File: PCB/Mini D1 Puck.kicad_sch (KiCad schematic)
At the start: 20 parts, among them J1 Regulator, J2 Charger, M1 VI1, M2 VI2, M3 VI3, M4 VI4, Q1 2N2222, Q2 2N2222, SW1 SW_SPDT, SW2 RST SW, U1 WEMOS_D1_mini

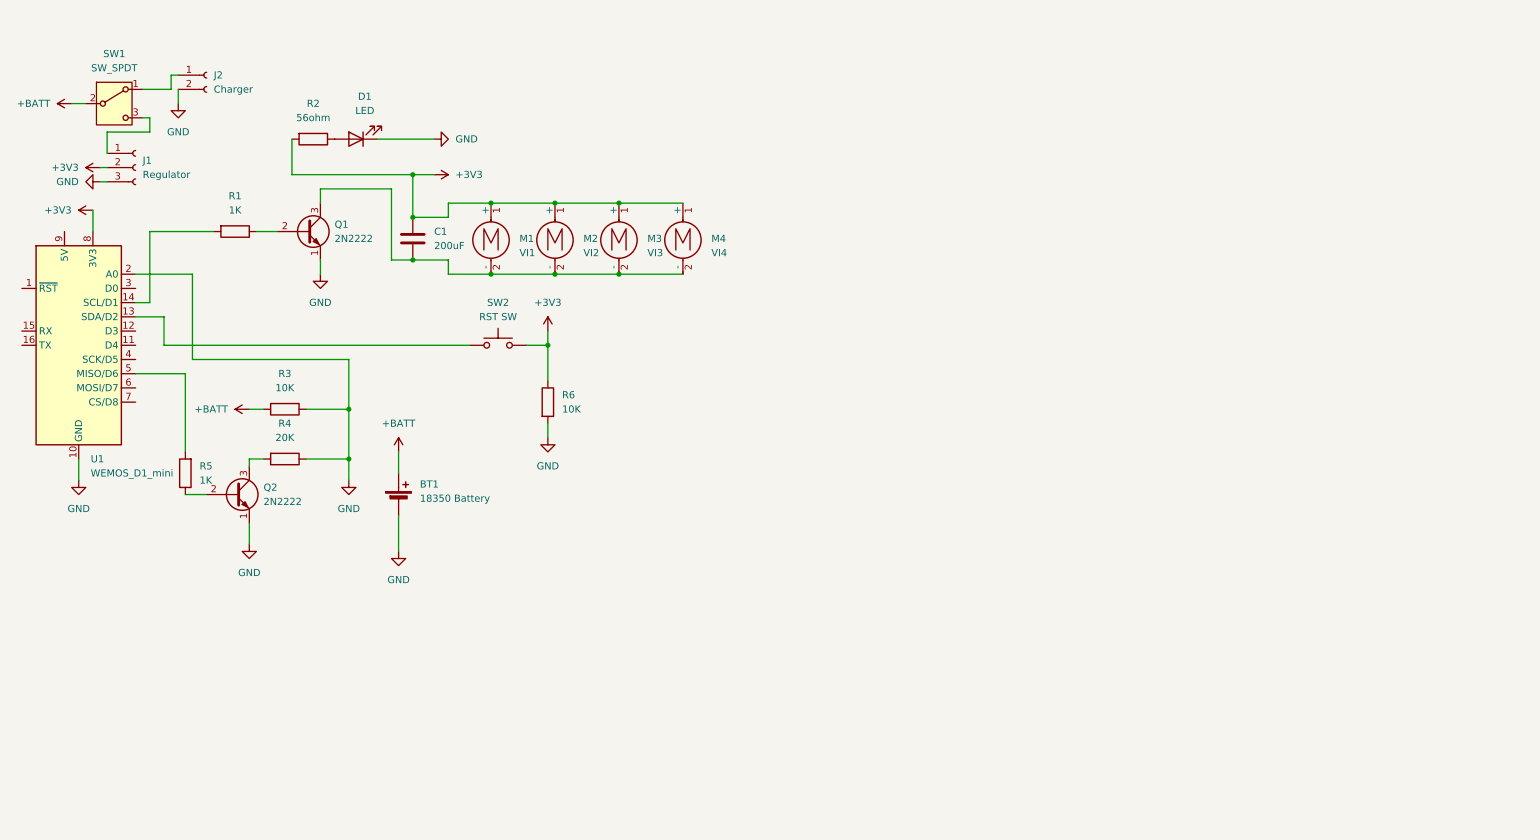
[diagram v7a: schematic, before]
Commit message: Work on new schematic, up minimum voltage in firmware
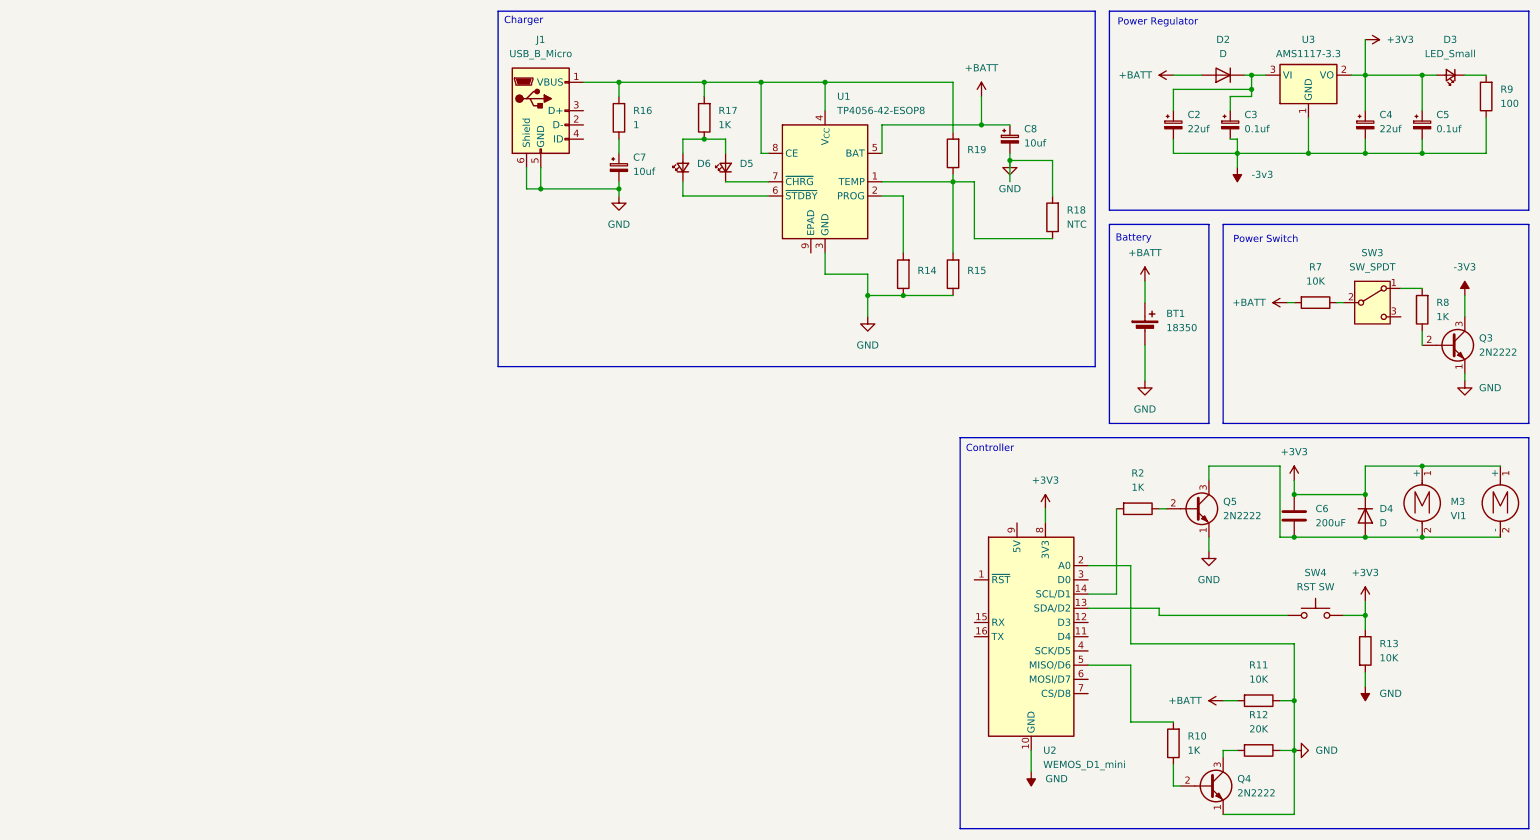
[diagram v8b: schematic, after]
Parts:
- removed C1: 200uF, symbol Device:C
- removed D1: LED, symbol Device:LED
- removed J1: Regulator, symbol Connector:Conn_01x03_Socket
- removed J2: Charger, symbol Connector:Conn_01x02_Socket
- removed M1: VI1, symbol Motor:Motor_DC
- removed M2: VI2, symbol Motor:Motor_DC
- removed Q1, Q2: 2N2222, symbol Transistor_BJT:Q_NPN_EBC
- removed R1, R5: 1K, symbol Device:R
- removed R3, R6: 10K, symbol Device:R
- removed R4: 20K, symbol Device:R
- removed SW1: SW_SPDT, symbol Switch:SW_SPDT
- removed SW2: RST SW, symbol Switch:SW_Push
- removed U1: WEMOS_D1_mini, RF_Module:WEMOS_D1_mini_light, symbol RF_Module:WEMOS_D1_mini
- added C2, C4: 22uf, symbol Device:C_Polarized_Small
- added C3, C5: 0.1uf, symbol Device:C_Polarized_Small
- added C6: 200uF, symbol Device:C
- added C7, C8: 10uf, symbol Device:C_Polarized_Small
- added D2, D4: D, symbol Device:D
- added D3: LED_Small, symbol Device:LED_Small
- added D5, D6: ~, symbol Device:LED_Small
- added J1: USB_B_Micro, symbol Connector:USB_B_Micro
- added Q3, Q4, Q5: 2N2222, symbol Transistor_BJT:Q_NPN_EBC
- added R10, R17, R8: 1K, symbol Device:R
- added R11, R13, R7: 10K, symbol Device:R
- added R12: 20K, symbol Device:R
- added R14, R15, R19: ~, symbol Device:R
- added R16: 1, symbol Device:R
- added R18: NTC, symbol Device:R
- added R9: 100, symbol Device:R
- added SW3: SW_SPDT, symbol Switch:SW_SPDT
- added SW4: RST SW, symbol Switch:SW_Push
- added U1: TP4056-42-ESOP8, Package_SO:SOIC-8-1EP_3.9x4.9mm_P1.27mm_EP2.41x3.3mm_ThermalVias, symbol Battery_Management:TP4056-42-ESOP8
- added U2: WEMOS_D1_mini, RF_Module:WEMOS_D1_mini_light, symbol RF_Module:WEMOS_D1_mini
- added U3: AMS1117-3.3, Package_TO_SOT_SMD:SOT-223-3_TabPin2, symbol Regulator_Linear:AMS1117-3.3
- BT1: value 18350 Battery -> 18350
- M3: value VI3 -> VI1
- M4: value VI4 -> VI2
- R2: value 56ohm -> 1K
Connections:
- net +3V3: now also C4.1, C5.1, C6.1, D3.2 (A), D4.1 (K), R13.1, SW4.2, U2.8 (3V3), U3.2 (VO); no longer R2.2
- net +BATT: now also C8.1, D2.2 (A), R11.2, R7.2, U1.5 (BAT)
- net GND: now also C7.2, C8.2, J1.5 (GND), J1.6 (Shield), Q3.1 (E), Q4.1 (E), Q5.1 (E), R11.1, R12.1, R13.2, R14.1, R15.1, R18.2, U1.3 (GND), U2.10 (GND), U2.2 (A0)
- net at R2.1: now also Q5.2 (B)
- net at M3.2 (-), M4.2 (-): now also C6.2, D4.2 (A), Q5.3 (C)
- new net: C2.1, C3.1, D2.1 (K), U3.3 (VI)
- new net: D3.1 (K), R9.2
- new net: Q3.2 (B), R8.1
- new net: R8.2, SW3.1 (A)
- new net: D5.1 (K), U1.7 (~{CHRG})
- new net: D5.2 (A), D6.2 (A), R17.1
- new net: J1.1 (VBUS), R16.2, R17.2, R19.2, U1.4 (V_{CC}), U1.8 (CE)
- new net: C7.1, R16.1
- new net: Q4.3 (C), R12.2
- new net: SW4.1, U2.13 (SDA/D2)
- new net: R2.2, U2.14 (SCL/D1)
- new net: R10.2, U2.5 (MISO/D6)
- new net: R7.1, SW3.2 (B)
- new net: Q4.2 (B), R10.1
- new net: R15.2, R18.1, R19.1, U1.1 (TEMP)
- new net: R14.2, U1.2 (PROG)
- new net: D6.1 (K), U1.6 (~{STDBY})
- new net -3V3: Q3.3 (C)
- new net -3v3: C2.2, C3.2, C4.2, C5.2, R9.1, U3.1 (GND)
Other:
- note added: "Battery"
- note added: "Charger"
- note added: "Controller"
- note added: "Power Regulator"
- note added: "Power Switch"
- moved on the sheet: BT1
